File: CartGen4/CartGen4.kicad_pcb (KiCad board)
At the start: 4 copper layers, 52.8 x 60.9 mm, 81 parts, among them J1 MEM2080-00-128-00-A, J2 Conn_01x05_Male, J3 Conn_02x09_Odd_Even, SW1 EVQ-P7A01P, U1 TPS65266-1RHBR, U10 IS25WP080D-JNLE, U11 DS1391U-33+, U2 SN74LV1T34DCKR, U3 SIT8008BI-73-33E-33.333333G, U4 NXS0108BQX, U5 AS1C8M16PL-70BIN, U6 NXS0108BQX, U7 NXS0108BQX, U8 NXS0104BQX, U9 LFXP2-8E-5MN132C, Y1 FC-135R 32.7680KA-E5

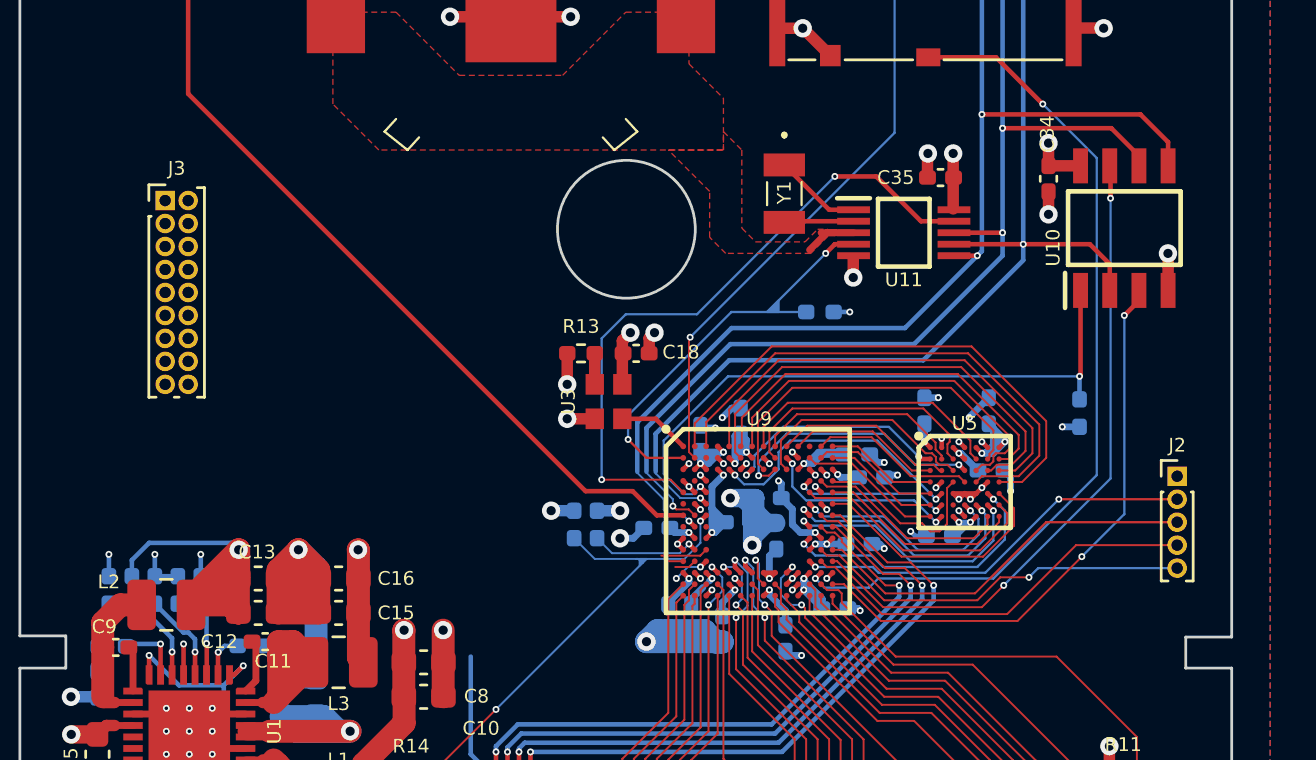
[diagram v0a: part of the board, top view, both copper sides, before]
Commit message: Switched from 1.00mm to 1.27mm pin headers
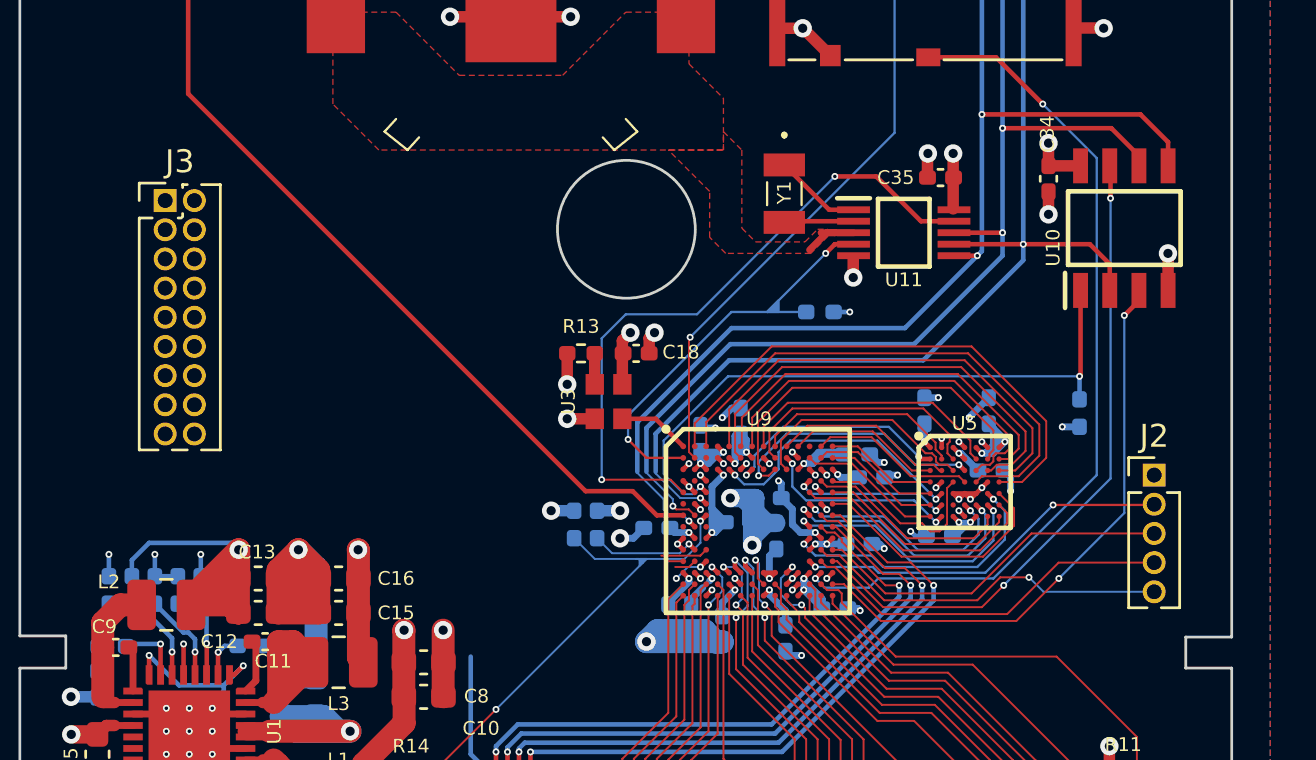
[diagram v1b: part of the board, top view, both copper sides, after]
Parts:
- J2: footprint Connector_PinHeader_1.00mm:PinHeader_1x05_P1.00mm_Vertical -> Connector_PinHeader_1.27mm:PinHeader_1x05_P1.27mm_Vertical
- J3: footprint Connector_PinHeader_1.00mm:PinHeader_2x09_P1.00mm_Vertical -> Connector_PinHeader_1.27mm:PinHeader_2x09_P1.27mm_Vertical
- moved J2 1.00 mm to (89.0, 71.7)
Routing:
- net FPGA_JTAG_TDI: track 17.7 -> 16.4 mm
- net FPGA_JTAG_TCK: track 17.2 -> 15.9 mm
- net FPGA_JTAG_TMS: track 17.5 -> 16.4 mm
- net FPGA_JTAG_TDO: track 17.0 -> 16.1 mm

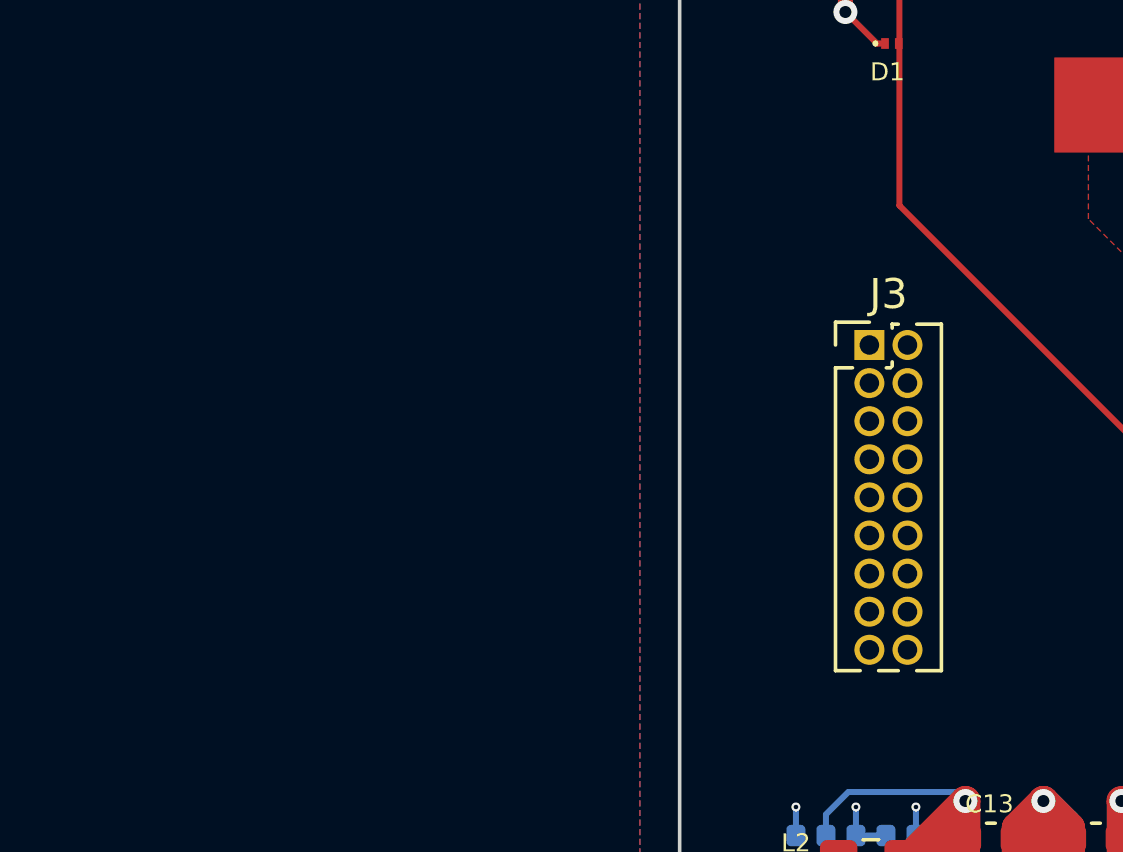
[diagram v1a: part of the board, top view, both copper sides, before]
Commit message: Changed J3 to SMD header
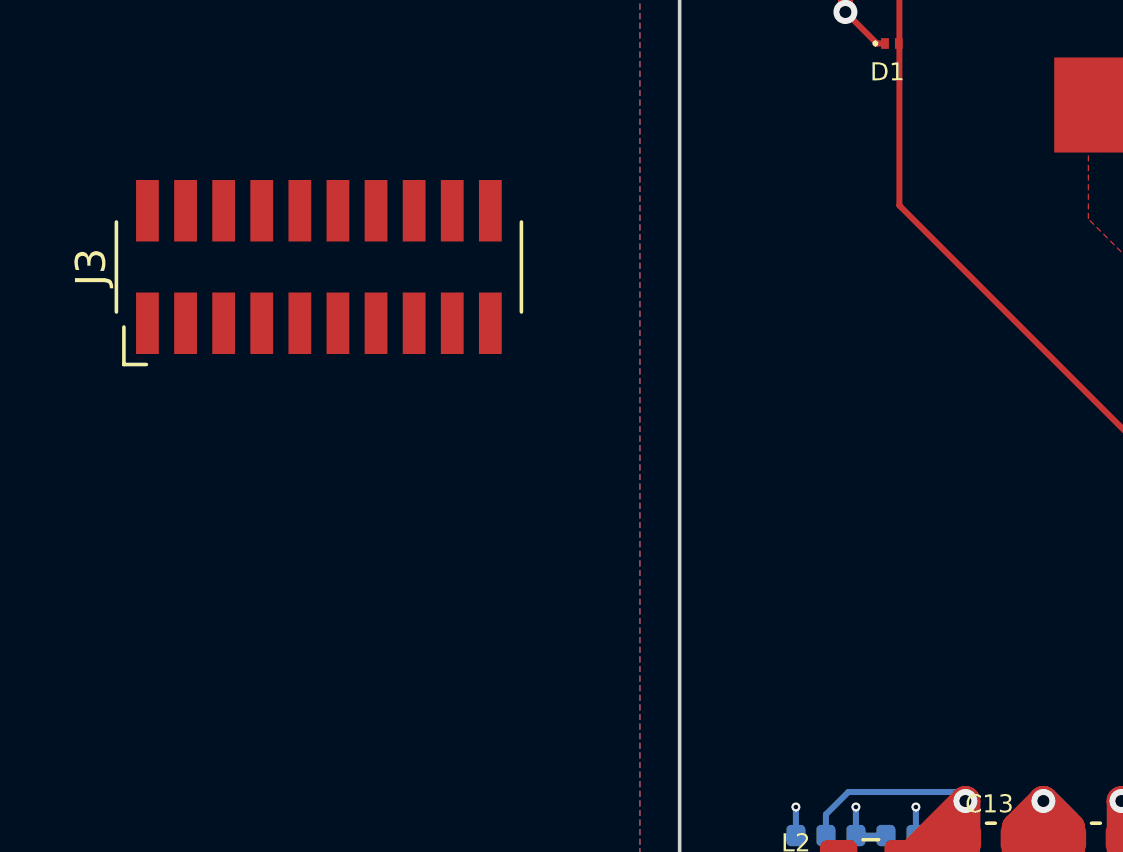
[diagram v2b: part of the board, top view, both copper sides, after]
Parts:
- J3: value Conn_02x09_Odd_Even -> Conn_02x10_Odd_Even; footprint Connector_PinHeader_1.27mm:PinHeader_2x09_P1.27mm_Vertical -> Connector:Conn_02x10
- moved J3 18.5 mm to (27.6, 57.1)
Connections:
- J3 pad 10: FPGA_USER3 -> FPGA_USER4
- J3 pad 12: FPGA_USER2 -> FPGA_USER3
- J3 pad 14: FPGA_USER1 -> FPGA_USER2
- J3 pad 15: FPGA_SOFT_RST# -> FPGA_DONE
- J3 pad 16: FPGA_USER0 -> FPGA_USER1
- J3 pad 17: GB_AUDIO -> FPGA_SOFT_RST#
- J3 pad 18: +3V3 -> FPGA_USER0
- J3 pad 2: FPGA_DONE -> GND
- J3 pad 4: FPGA_USER6 -> GB_AUDIO
- J3 pad 6: FPGA_USER5 -> FPGA_USER6
- J3 pad 8: FPGA_USER4 -> FPGA_USER5

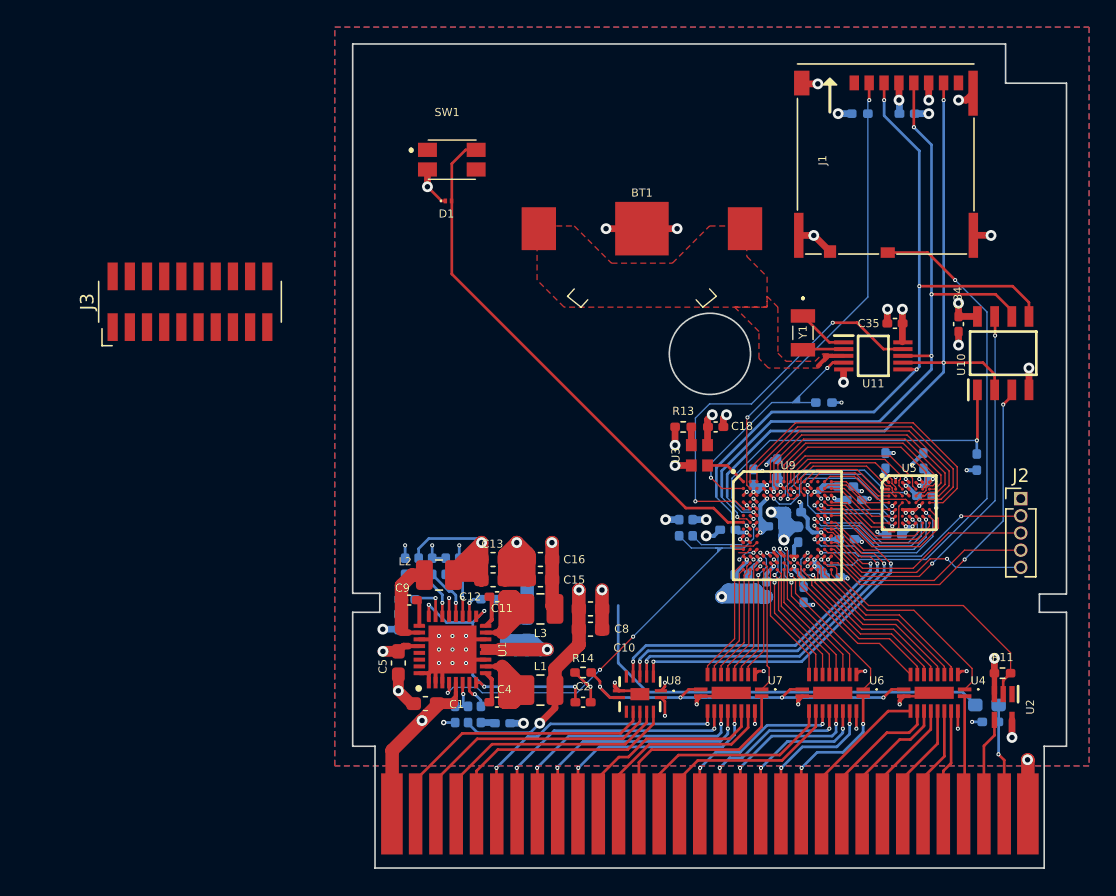
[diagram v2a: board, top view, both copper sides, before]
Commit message: Routed expansion port
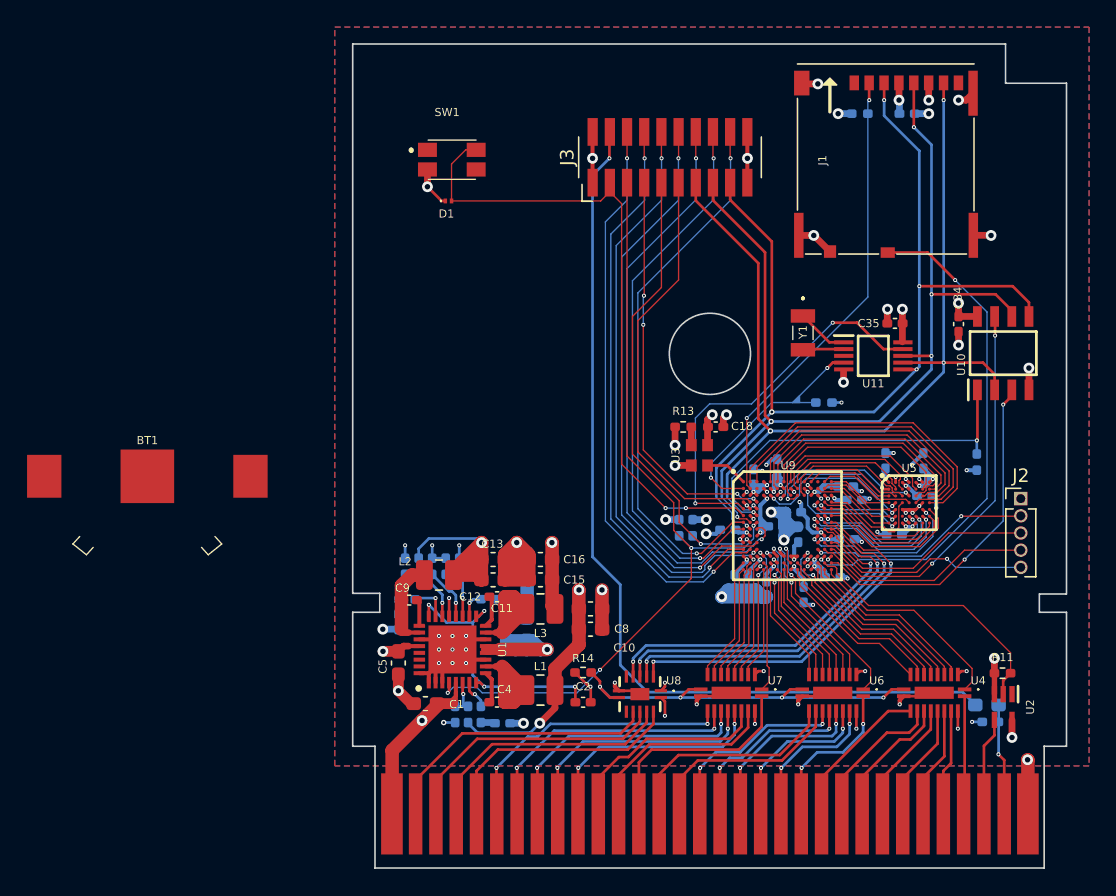
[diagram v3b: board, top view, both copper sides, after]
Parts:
- moved BT1 40.9 mm to (24.4, 70.0)
- moved J3 37.0 mm to (63.1, 46.4)
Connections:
- J3 pad 11: FPGA_TOE -> FPGA_CSSPISN
- J3 pad 13: PS_PGOOD -> FPGA_SPI_MISO
- J3 pad 15: FPGA_DONE -> FPGA_SPI_CLK
- J3 pad 17: FPGA_SOFT_RST# -> FPGA_SPI_MOSI
- J3 pad 3: FPGA_CSSPISN -> FPGA_SOFT_RST#
- J3 pad 5: FPGA_SPI_MISO -> PS_PGOOD
- J3 pad 7: FPGA_SPI_CLK -> FPGA_DONE
- J3 pad 9: FPGA_SPI_MOSI -> FPGA_TOE
- U9 pad K3: FPGA_USER5 -> FPGA_USER3
- U9 pad L1: FPGA_USER3 -> FPGA_USER5
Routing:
- net FPGA_USER2: track 0.00 -> 44.0 mm, vias 0 -> 2
- net FPGA_USER6: track 0.95 -> 43.2 mm, vias 0 -> 2
- net FPGA_USER3: track 0.67 -> 42.4 mm, vias 0 -> 2
- net FPGA_USER4: track 1.61 -> 42.8 mm
- net FPGA_USER1: track 0.00 -> 41.0 mm, vias 0 -> 2
- net FPGA_USER0: track 0.00 -> 40.8 mm, vias 0 -> 2
- net FPGA_USER5: track 2.06 -> 42.9 mm, vias 0 -> 2
- net GB_AUDIO: track 31.9 -> 68.2 mm, vias 0 -> 1
- net FPGA_CSSPISN: track 0.00 -> 31.0 mm
- net FPGA_TOE: track 4.79 -> 34.4 mm, vias 1 -> 2
- net FPGA_DONE: track 0.36 -> 29.8 mm, vias 1 -> 4
- net PS_PGOOD: track 33.6 -> 61.3 mm
- net FPGA_SPI_MISO: track 53.3 -> 73.9 mm, vias 3 -> 4
- net FPGA_SPI_CLK: track 54.3 -> 73.7 mm, vias 4 -> 5
- net FPGA_SPI_MOSI: track 56.7 -> 75.0 mm, vias 4 -> 5
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- removed copper zone on F.Cu, net +VBAT

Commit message: Routed VBAT
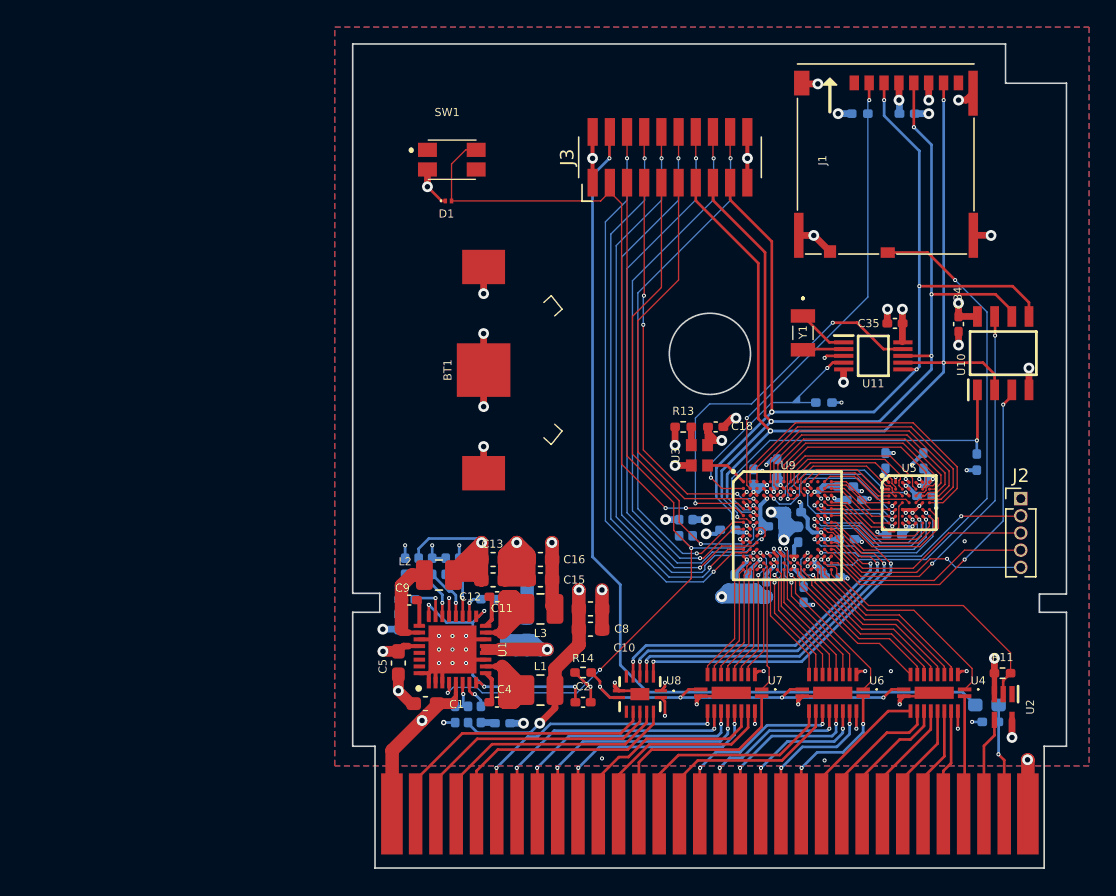
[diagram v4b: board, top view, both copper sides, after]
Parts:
- moved BT1 26.1 mm to (49.3, 62.1), turned to -90 degrees
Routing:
- net GND: track 130.6 -> 136.2 mm, vias 77 -> 83
- net +VBAT: track 0.00 -> 5.42 mm, vias 0 -> 3
- net +1V8: track 38.6 -> 40.0 mm
- added copper zone on In1.Cu, net +VBAT

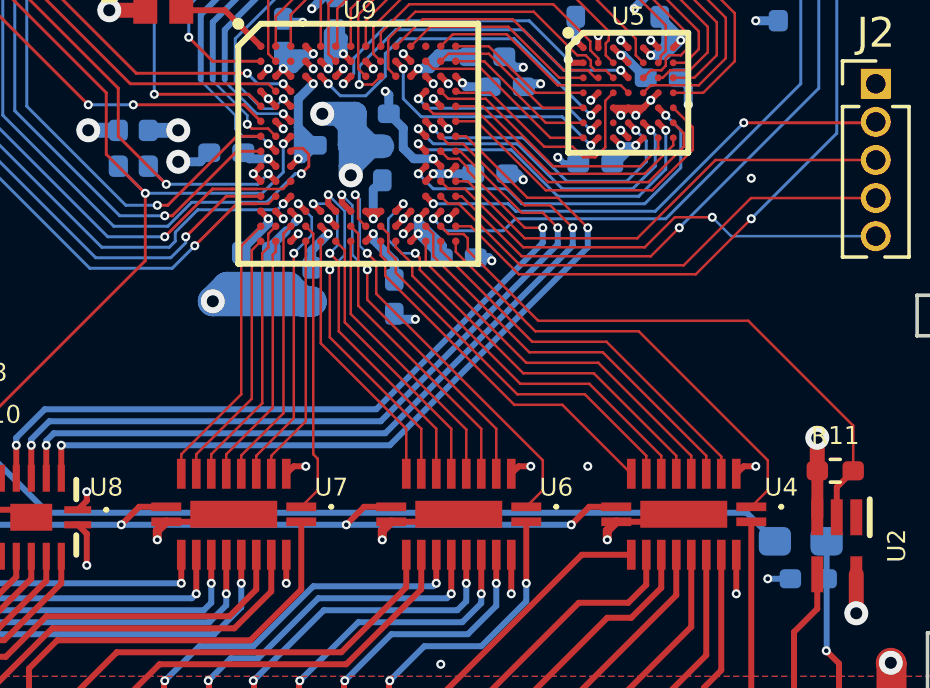
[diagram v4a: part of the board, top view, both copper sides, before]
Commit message: Increased clearances between GB lines
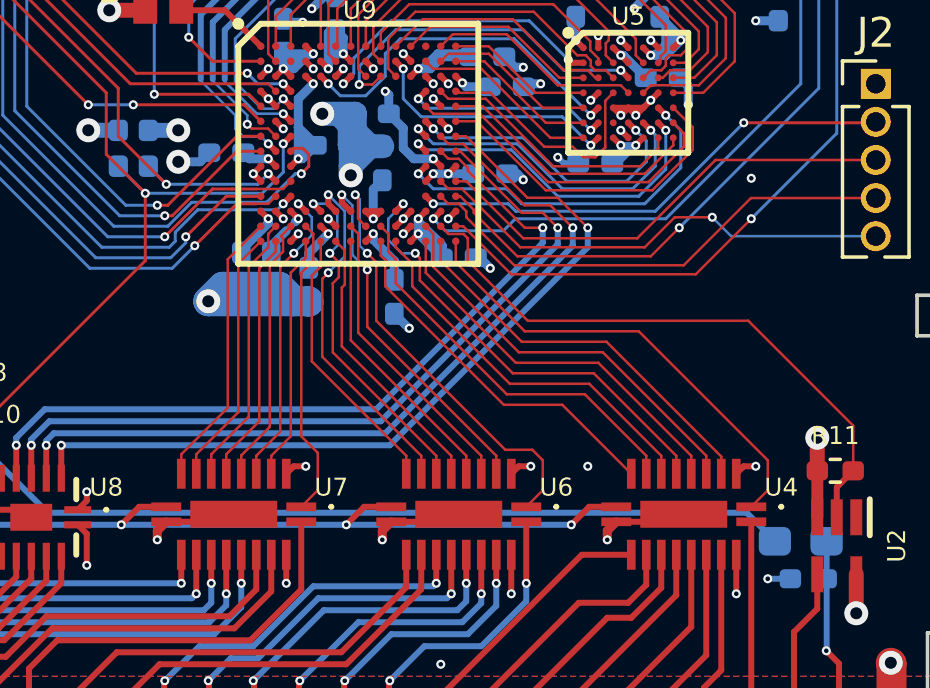
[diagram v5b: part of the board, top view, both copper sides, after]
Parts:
- moved C25 0.10 mm to (70.1, 78.3)
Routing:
- net GB_ADDR15: track 14.4 -> 14.9 mm
